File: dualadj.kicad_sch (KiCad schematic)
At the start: 12 parts, among them J8 Conn_01x02_Female, J9 Conn_01x02_Female, U1 LM317_TO-220, U2 LM337_TO220

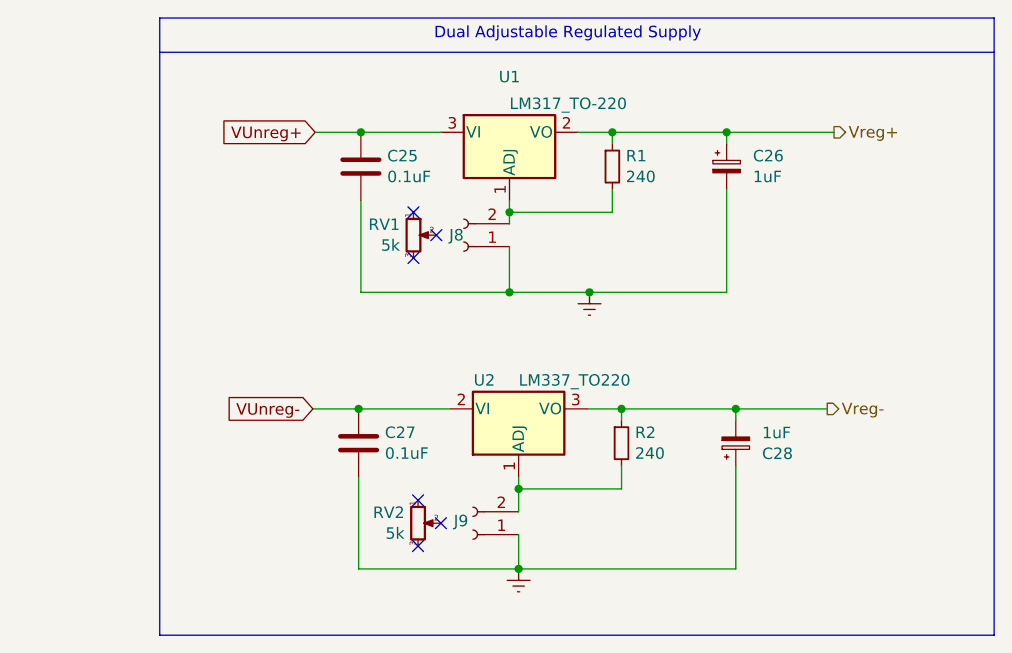
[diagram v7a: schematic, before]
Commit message: new EMC-EMI layout with improved suppression
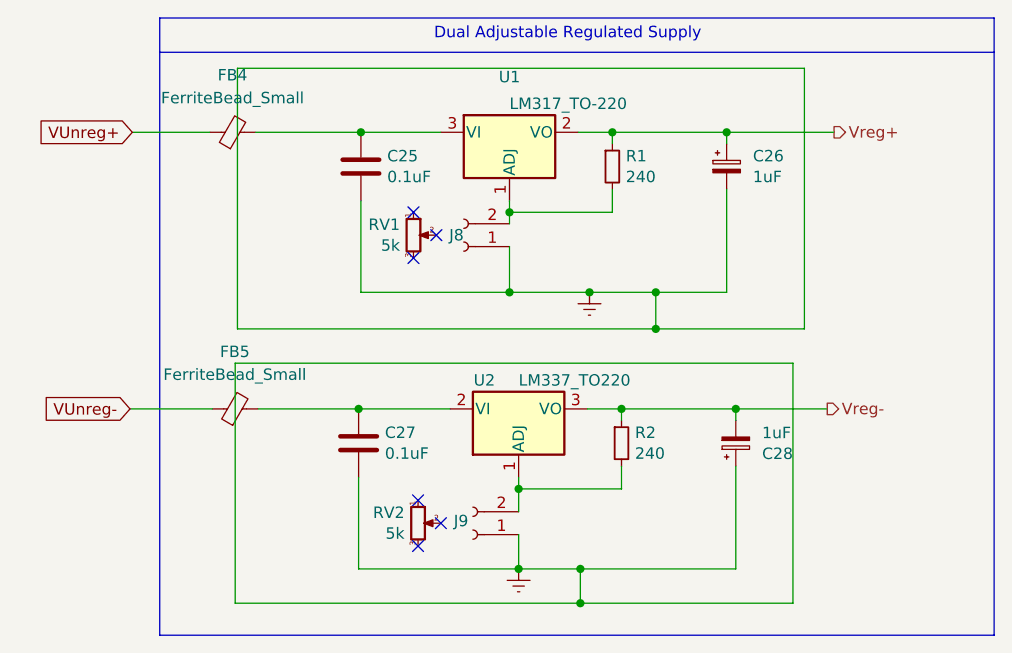
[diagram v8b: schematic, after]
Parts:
- added FB4, FB5: FerriteBead_Small, Inductor_SMD:L_0603_1608Metric, symbol Device:FerriteBead_Small
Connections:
- net VUnreg+: now also FB4.1; no longer C25.1, U1.3 (VI)
- net VUnreg-: now also FB5.1; no longer C27.1, U2.2 (VI)
- new net: C25.1, FB4.2, U1.3 (VI)
- new net: C27.1, FB5.2, U2.2 (VI)
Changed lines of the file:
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@@
   (junction (at 136.652 81.28) (diameter 0) (color 0 0 0 0)
   )
+  (junction (at 144.526 124.714) (diameter 0) (color 0 0 0 0)
+  )
   (junction (at 120.142 72.39) (diameter 0) (color 0 0 0 0)
   )
   (junction (at 136.652 90.17) (diameter 0) (color 0 0 0 0)
   )
+  (junction (at 152.908 94.234) (diameter 0) (color 0 0 0 0)
+  )
   (junction (at 149.098 103.124) (diameter 0) (color 0 0 0 0)
   )
@@
   )
   (junction (at 137.668 112.014) (diameter 0) (color 0 0 0 0)
+  )
+  (junction (at 144.526 120.904) (diameter 0) (color 0 0 0 0)
+  )
+  (junction (at 152.908 90.17) (diameter 0) (color 0 0 0 0)
   )
   (junction (at 160.782 72.39) (diameter 0) (color 0 0 0 0)
@@
     (stroke (width 0) (type default) (color 0 0 0 0))
   )
-  (wire (pts (xy 115.062 72.39) (xy 120.142 72.39))
+  (wire (pts (xy 94.742 72.39) (xy 103.378 72.39))
+    (stroke (width 0) (type default) (color 0 0 0 0))
+  )
+  (wire (pts (xy 106.172 98.044) (xy 106.172 124.714))
     (stroke (width 0) (type default) (color 0 0 0 0))
   )
@@
     (stroke (width 0) (type default) (color 0 0 0 0))
   )
+  (wire (pts (xy 106.172 124.714) (xy 144.526 124.714))
+    (stroke (width 0) (type default) (color 0 0 0 0))
+  )
   (wire (pts (xy 149.098 112.014) (xy 149.098 109.474))
     (stroke (width 0) (type default) (color 0 0 0 0))
@@
     (stroke (width 0) (type default) (color 0 0 0 0))
   )
+  (wire (pts (xy 108.458 72.39) (xy 120.142 72.39))
+    (stroke (width 0) (type default) (color 0 0 0 0))
+  )
   (polyline (pts (xy 97.79 59.69) (xy 97.79 128.27))
     (stroke (width 0) (type default) (color 0 0 0 0))
@@
     (stroke (width 0) (type default) (color 0 0 0 0))
   )
-  (wire (pts (xy 145.542 90.17) (xy 160.782 90.17))
+  (wire (pts (xy 145.542 90.17) (xy 152.908 90.17))
+    (stroke (width 0) (type default) (color 0 0 0 0))
+  )
+  (wire (pts (xy 106.426 94.234) (xy 152.908 94.234))
     (stroke (width 0) (type default) (color 0 0 0 0))
   )
@@
     (stroke (width 0) (type default) (color 0 0 0 0))
   )
+  (wire (pts (xy 144.526 124.714) (xy 168.148 124.714))
+    (stroke (width 0) (type default) (color 0 0 0 0))
+  )
+  (wire (pts (xy 152.908 94.234) (xy 169.418 94.234))
+    (stroke (width 0) (type default) (color 0 0 0 0))
+  )
   (wire (pts (xy 148.082 73.66) (xy 148.082 72.39))
     (stroke (width 0) (type default) (color 0 0 0 0))
@@
     (stroke (width 0) (type default) (color 0 0 0 0))
   )
+  (wire (pts (xy 152.908 90.17) (xy 160.782 90.17))
+    (stroke (width 0) (type default) (color 0 0 0 0))
+  )
   (wire (pts (xy 161.798 103.124) (xy 161.798 104.394))
     (stroke (width 0) (type default) (color 0 0 0 0))
   )
+  (wire (pts (xy 168.148 124.714) (xy 168.148 98.044))
+    (stroke (width 0) (type default) (color 0 0 0 0))
+  )
+  (wire (pts (xy 106.426 65.278) (xy 106.426 94.234))
+    (stroke (width 0) (type default) (color 0 0 0 0))
+  )
   (wire (pts (xy 161.798 109.474) (xy 161.798 120.904))
     (stroke (width 0) (type default) (color 0 0 0 0))
   )
-  (wire (pts (xy 137.668 120.904) (xy 161.798 120.904))
+  (wire (pts (xy 169.418 94.234) (xy 169.418 65.278))
+    (stroke (width 0) (type default) (color 0 0 0 0))
+  )
+  (wire (pts (xy 103.632 103.124) (xy 94.488 103.124))
+    (stroke (width 0) (type default) (color 0 0 0 0))
+  )
+  (wire (pts (xy 137.668 120.904) (xy 144.526 120.904))
     (stroke (width 0) (type default) (color 0 0 0 0))
   )
@@
     (stroke (width 0) (type default) (color 0 0 0 0))
   )
+  (wire (pts (xy 106.172 98.044) (xy 168.148 98.044))
+    (stroke (width 0) (type default) (color 0 0 0 0))
+  )
   (wire (pts (xy 145.288 103.124) (xy 149.098 103.124))
     (stroke (width 0) (type default) (color 0 0 0 0))
@@
     (stroke (width 0) (type default) (color 0 0 0 0))
   )
+  (wire (pts (xy 144.526 120.904) (xy 161.798 120.904))
+    (stroke (width 0) (type default) (color 0 0 0 0))
+  )
   (wire (pts (xy 136.652 90.17) (xy 145.542 90.17))
     (stroke (width 0) (type default) (color 0 0 0 0))
@@
     (stroke (width 0) (type default) (color 0 0 0 0))
   )
-  (wire (pts (xy 119.888 103.124) (xy 114.808 103.124))
+  (wire (pts (xy 119.888 103.124) (xy 108.712 103.124))
     (stroke (width 0) (type default) (color 0 0 0 0))
   )
@@
     (stroke (width 0) (type default) (color 0 0 0 0))
   )
+  (wire (pts (xy 144.526 120.904) (xy 144.526 124.714))
+    (stroke (width 0) (type default) (color 0 0 0 0))
+  )
   (wire (pts (xy 144.272 72.39) (xy 148.082 72.39))
+    (stroke (width 0) (type default) (color 0 0 0 0))
+  )
+  (wire (pts (xy 152.908 94.234) (xy 152.908 90.17))
+    (stroke (width 0) (type default) (color 0 0 0 0))
+  )
+  (wire (pts (xy 106.426 65.278) (xy 169.418 65.278))
     (stroke (width 0) (type default) (color 0 0 0 0))
   )
@@
     (effects (font (size 1.27 1.27)) (justify left bottom))
   )
-  (global_label "VUnreg+" (shape input) (at 115.062 72.39 180) (fields_autoplaced)
+  (global_label "VUnreg+" (shape input) (at 94.742 72.39 180) (fields_autoplaced)
     (effects (font (size 1.27 1.27)) (justify right))
-    (property "Intersheet References" "${INTERSHEET_REFS}" (id 0) (at 104.5735 72.3106 0)
+    (property "Intersheet References" "${INTERSHEET_REFS}" (id 0) (at 84.2535 72.3106 0)
       (effects (font (size 1.27 1.27)) (justify right))
     )
   )
-  (global_label "VUnreg-" (shape input) (at 114.808 103.124 180) (fields_autoplaced)
+  (global_label "VUnreg-" (shape input) (at 94.488 103.124 180) (fields_autoplaced)
     (effects (font (size 1.27 1.27)) (justify right))
-    (property "Intersheet References" "${INTERSHEET_REFS}" (id 0) (at 104.3195 103.0446 0)
+    (property "Intersheet References" "${INTERSHEET_REFS}" (id 0) (at 83.9995 103.0446 0)
       (effects (font (size 1.27 1.27)) (justify right))
     )
@@
     (pin "3")
   )
+  (symbol (lib_id "Device:FerriteBead_Small") (at 106.172 103.124 90) (unit 1)
+    (in_bom yes) (on_board yes) (fields_autoplaced)
+    (property "Reference" "FB5" (id 0) (at 106.1339 96.774 90))
+    (property "Value" "FerriteBead_Small" (id 1) (at 106.1339 99.314 90))
+    (property "Footprint" "Inductor_SMD:L_0603_1608Metric" (id 2) (at 106.172 104.902 90)
+      (effects (font (size 1.27 1.27)) hide)
+    )
+    (property "Datasheet" "~" (id 3) (at 106.172 103.124 0)
+      (effects (font (size 1.27 1.27)) hide)
+    )
+    (pin "1")
+    (pin "2")
+  )
+  (symbol (lib_id "Device:FerriteBead_Small") (at 105.918 72.39 90) (unit 1)
+    (in_bom yes) (on_board yes) (fields_autoplaced)
+    (property "Reference" "FB4" (id 0) (at 105.8799 66.04 90))
+    (property "Value" "FerriteBead_Small" (id 1) (at 105.8799 68.58 90))
+    (property "Footprint" "Inductor_SMD:L_0603_1608Metric" (id 2) (at 105.918 74.168 90)
+      (effects (font (size 1.27 1.27)) hide)
+    )
+    (property "Datasheet" "~" (id 3) (at 105.918 72.39 0)
+      (effects (font (size 1.27 1.27)) hide)
+    )
+    (pin "1")
+    (pin "2")
+  )
   (symbol (lib_id "Device:C") (at 119.888 106.934 0) (unit 1)
